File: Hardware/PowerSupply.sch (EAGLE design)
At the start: 21 parts, among them Q1 IRF730, T1 BC857, U1 MC34063

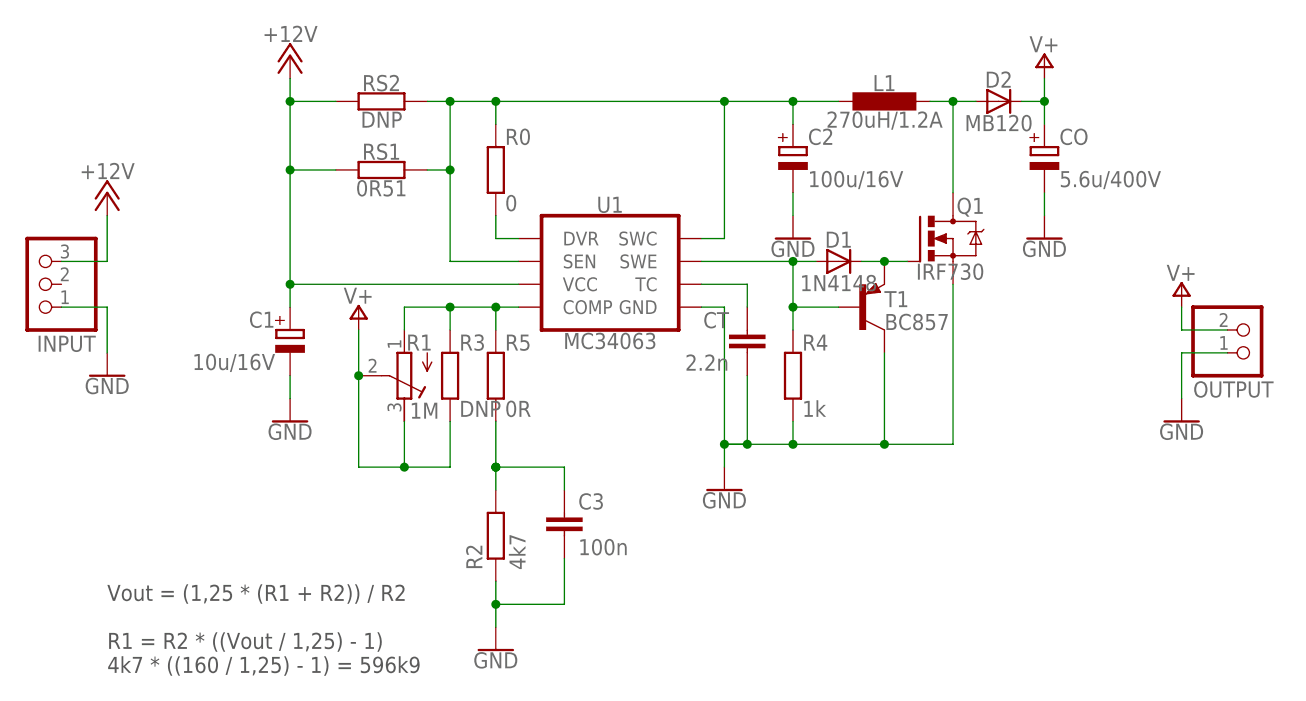
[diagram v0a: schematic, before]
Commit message: renamed power supply design files
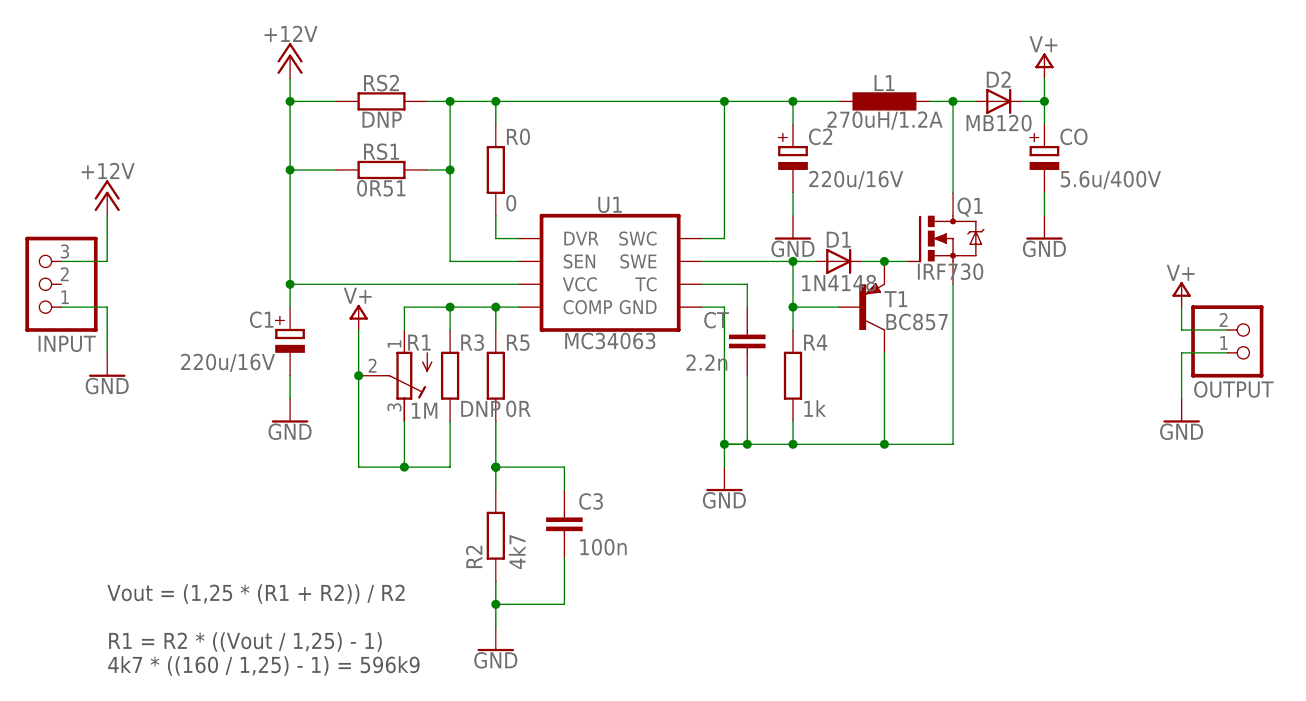
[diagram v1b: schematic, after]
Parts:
- C1: value 10u/16V -> 220u/16V
- C2: value 100u/16V -> 220u/16V
- Q1: SPICEPREFIX (none) -> Q
- U1: SPICEPREFIX (none) -> X
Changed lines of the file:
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@@
 <parts>
 <part name="L1" library="NixieClock" library_urn="urn:adsk.eagle:library:7479626" deviceset="TC-PIS4728" device="" package3d_urn="urn:adsk.eagle:package:7646352/3" value="270uH/1.2A"/>
-<part name="U1" library="NixieClock" library_urn="urn:adsk.eagle:library:7479626" deviceset="MC34063" device="" package3d_urn="urn:adsk.eagle:package:7646370/1"/>
+<part name="U1" library="NixieClock" library_urn="urn:adsk.eagle:library:7479626" deviceset="MC34063" device="" package3d_urn="urn:adsk.eagle:package:7646370/1">
+<attribute name="SPICEPREFIX" value="X"/>
+</part>
 <part name="CT" library="rcl" library_urn="urn:adsk.eagle:library:334" deviceset="C-EU" device="C0603K" package3d_urn="urn:adsk.eagle:package:23680/2" value="2.2n"/>
 <part name="RS2" library="rcl" library_urn="urn:adsk.eagle:library:334" deviceset="R-EU_" device="R2512" package3d_urn="urn:adsk.eagle:package:23545/2" value="DNP"/>
@@
 <part name="P+2" library="supply1" library_urn="urn:adsk.eagle:library:371" deviceset="V+" device=""/>
 <part name="GND1" library="supply1" library_urn="urn:adsk.eagle:library:371" deviceset="GND" device=""/>
-<part name="C1" library="rcl" library_urn="urn:adsk.eagle:library:334" deviceset="CPOL-EU" device="140CLH-0810" package3d_urn="urn:adsk.eagle:package:23392/1" value="10u/16V"/>
+<part name="C1" library="rcl" library_urn="urn:adsk.eagle:library:334" deviceset="CPOL-EU" device="140CLH-0810" package3d_urn="urn:adsk.eagle:package:23392/1" value="220u/16V"/>
 <part name="GND2" library="supply1" library_urn="urn:adsk.eagle:library:371" deviceset="GND" device=""/>
 <part name="GND3" library="supply1" library_urn="urn:adsk.eagle:library:371" deviceset="GND" device=""/>
@@
 <part name="P+5" library="supply1" library_urn="urn:adsk.eagle:library:371" deviceset="+12V" device=""/>
 <part name="GND5" library="supply1" library_urn="urn:adsk.eagle:library:371" deviceset="GND" device=""/>
-<part name="Q1" library="transistor-power" library_urn="urn:adsk.eagle:library:400" deviceset="IRF740" device="" package3d_urn="urn:adsk.eagle:package:29484/3" value="IRF730"/>
-<part name="C2" library="rcl" library_urn="urn:adsk.eagle:library:334" deviceset="CPOL-EU" device="140CLH-0810" package3d_urn="urn:adsk.eagle:package:23392/1" value="100u/16V"/>
+<part name="Q1" library="transistor-power" library_urn="urn:adsk.eagle:library:400" deviceset="IRF740" device="" package3d_urn="urn:adsk.eagle:package:29484/3" value="IRF730">
+<attribute name="SPICEPREFIX" value="Q"/>
+</part>
+<part name="C2" library="rcl" library_urn="urn:adsk.eagle:library:334" deviceset="CPOL-EU" device="140CLH-0810" package3d_urn="urn:adsk.eagle:package:23392/1" value="220u/16V"/>
 <part name="C3" library="rcl" library_urn="urn:adsk.eagle:library:334" deviceset="C-EU" device="C0603K" package3d_urn="urn:adsk.eagle:package:23680/2" value="100n"/>
 <part name="R4" library="rcl" library_urn="urn:adsk.eagle:library:334" deviceset="R-EU_" device="R0603" package3d_urn="urn:adsk.eagle:package:23555/2" value="1k"/>
